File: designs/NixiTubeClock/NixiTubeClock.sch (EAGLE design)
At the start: 14 parts, among them IC1 74141N, IC2 74141N, IC3 74141N, IC4 74141N

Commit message: added nixi tube project
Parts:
- removed V1, V2: 74595N, NixieTube:74595N
- added IC5: 74HCT595D, NixieTube:74HCT595D
- added IC6: 74141N, NixieTube:74141N
- added SV1: (no value), con-lstb:MA08-1
- IC2: value 74141N -> 74HCT595D; device NixieTube:74141N -> NixieTube:74HCT595D
- R1, R2, R3: value (none) -> 12k
- R4: value 68Kh -> (none)
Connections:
- removed net N$1: IC2A.D, V11.QH*
- removed net N$10: IC3A.B, V21.QH
- removed net N$11: IC3A.C, V21.QG
- removed net N$12: IC3A.D, V21.QF
- removed net N$14: IC4A.B, V21.QD
- removed net N$2: IC2A.C, V11.QH
- removed net N$3: IC2A.B, V11.QG
- removed net N$33: AN1.6, IC1A.3
- removed net N$34: AN1.7, IC1A.2
- removed net N$37: AN3.9, IC3A.0
- removed net N$38: AN3.8, IC3A.1
- removed net N$39: AN3.7, IC3A.2
- removed net N$4: IC2A.A, V11.QF
- removed net N$40: AN3.6, IC3A.3
- removed net N$41: AN3.5, IC3A.4
- removed net N$42: AN3.4, IC3A.5
- removed net N$43: AN3.3, IC3A.6
- removed net N$44: AN3.2, IC3A.7
- removed net N$45: AN3.1, IC3A.8
- removed net N$46: AN3.0, IC3A.9
- removed net N$47: AN4.9, IC4A.0
- removed net N$48: AN4.8, IC4A.1
- removed net N$49: AN4.7, IC4A.2
- removed net N$5: IC1A.D, V11.QE
- removed net N$50: AN4.6, IC4A.3
- removed net N$51: AN4.5, IC4A.4
- removed net N$52: AN4.4, IC4A.5
- removed net N$53: AN4.3, IC4A.6
- removed net N$54: AN4.2, IC4A.7
- removed net N$55: AN4.1, IC4A.8
- removed net N$56: AN4.0, IC4A.9
- removed net N$6: IC1A.C, V11.QD
- removed net N$8: IC1A.A, V11.QB
- new net 170V: R1.2, R2.2, R3.2, R4.2, SV1.6
- new net DS: IC2A.SER, SV1.1
- new net N$100: AN4.A1, R4.1
- new net N$101: IC1A.A, IC2A.QA
- new net N$102: IC1A.B, IC2A.QB
- new net N$103: IC1A.C, IC2A.QC
- new net N$104: IC1A.D, IC2A.QD
- new net N$105: IC2A.QE, IC3A.A
- new net N$106: IC2A.QF, IC3A.B
- new net N$107: IC2A.QG, IC3A.C
- new net N$108: IC2A.QH, IC3A.D
- new net N$109: IC4A.A, IC5A.QA
- new net N$110: IC4A.B, IC5A.QB
- new net N$111: IC4A.C, IC5A.QC
- new net N$112: IC5A.QD
- new net N$113: IC5A.QE, IC6A.A
- new net N$114: IC5A.QF, IC6A.B
- new net N$115: IC5A.QG, IC6A.C
- new net N$116: IC5A.QH, IC6A.D
- new net N$66: AN3.3, IC4A.3
- new net N$67: AN3.4, IC4A.4
- new net N$68: AN3.5, IC4A.5
- new net N$69: AN3.6, IC4A.6
- new net N$70: AN3.7, IC4A.7
- new net N$71: AN3.8, IC4A.8
- new net N$72: AN3.9, IC4A.9
- new net N$73: AN4.0, IC6A.0
- new net N$74: AN4.1, IC6A.1
- new net N$75: AN4.2, IC6A.2
- new net N$76: AN4.3, IC6A.3
- new net N$91: AN4.4, IC6A.4
- new net N$92: AN4.5, IC6A.5
- new net N$93: AN4.6, IC6A.6
- new net N$94: AN4.7, IC6A.7
- new net N$95: AN4.8, IC6A.8
- new net N$96: AN4.9, IC6A.9
- new net N$97: AN1.A1, R1.1
- new net N$98: AN2.A1, R2.1
- new net N$99: AN3.A1, R3.1
- new net SHIFT_DATA: IC2A.QH*, IC5A.SER
- new net SH_CP: IC2A.SCK, IC5A.SCK, SV1.2
- new net ST_CP: IC2A.RCK, IC5A.RCK, SV1.3
- new net VCC: SV1.4
- net 5V: now also IC2A.SCL, IC5A.SCL; no longer IC1P.VCC, IC2P.VCC, IC3P.VCC, IC4P.VCC
- net GND: now also IC2A.G, IC5A.G, SV1.5, SV1.7, SV1.8; no longer IC1P.GND, IC2P.GND, IC3P.GND, IC4P.GND
- net N$13: now also AN1.2, IC1A.2; no longer IC4A.A, V21.QE
- net N$15: now also AN1.3, IC1A.3; no longer IC4A.C, V21.QC
- net N$16: now also AN1.4, IC1A.4; no longer IC4A.D, V21.QB
- net N$17: now also AN1.5, IC1A.5; no longer AN2.9, IC2A.0
- net N$18: now also AN1.6, IC1A.6; no longer AN2.8, IC2A.1
- net N$19: now also AN1.7, IC1A.7; no longer AN2.7, IC2A.2
- net N$20: now also AN1.8, IC1A.8; no longer AN2.6, IC2A.3
- net N$21: now also AN1.9, IC1A.9; no longer AN2.5, IC2A.4
- net N$22: now also AN2.0, IC3A.0; no longer AN2.4, IC2A.5
- net N$23: now also AN2.1, IC3A.1; no longer AN2.3, IC2A.6
- net N$24: now also IC3A.2; no longer IC2A.7
- net N$25: now also AN2.3, IC3A.3; no longer AN2.1, IC2A.8
- net N$26: now also AN2.4, IC3A.4; no longer AN2.0, IC2A.9
- net N$27: now also AN2.5, IC3A.5; no longer AN1.0, IC1A.9
- net N$28: now also AN2.6, IC3A.6; no longer AN1.1, IC1A.8
- net N$29: now also AN2.7, IC3A.7; no longer AN1.2, IC1A.7
- net N$30: now also AN2.8, IC3A.8; no longer AN1.3, IC1A.6
- net N$31: now also AN2.9, IC3A.9; no longer AN1.4, IC1A.5
- net N$32: now also AN3.0, IC4A.0; no longer AN1.5, IC1A.4
- net N$35: now also AN3.1, IC4A.1; no longer AN1.8, IC1A.1
- net N$36: now also AN3.2, IC4A.2; no longer AN1.9, IC1A.0
- net N$7: now also AN1.0, IC1A.0; no longer IC1A.B, V11.QC
- net N$9: now also AN1.1, IC1A.1; no longer IC3A.A, V21.QH*
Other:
- note added: "Nothing just Picture"

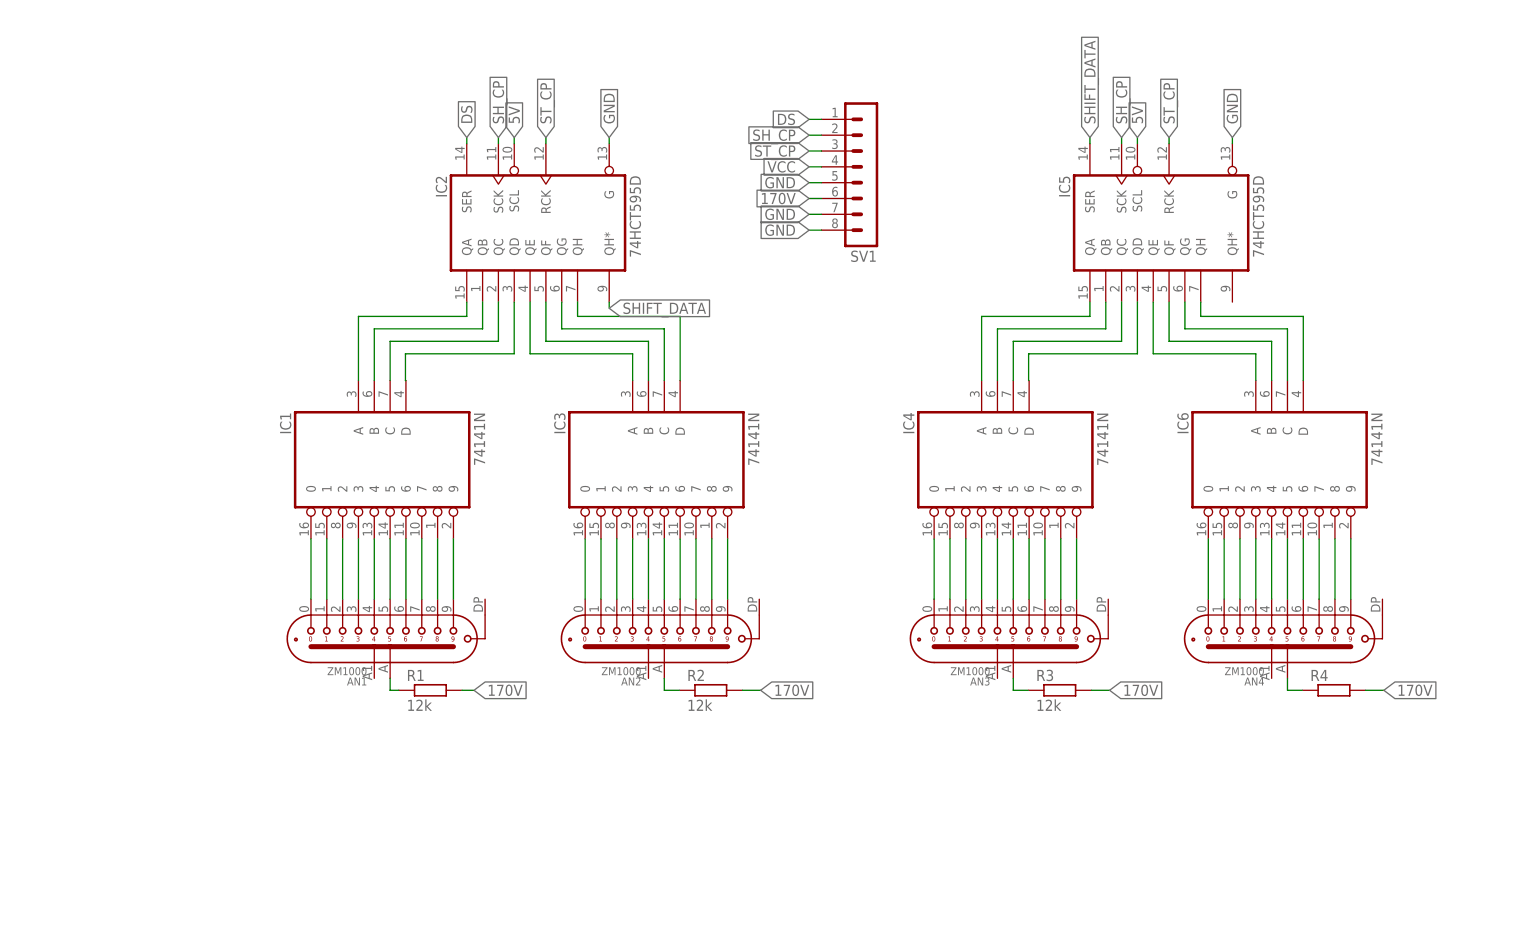
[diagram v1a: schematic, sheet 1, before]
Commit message: added parts for nixi clock final check during the week
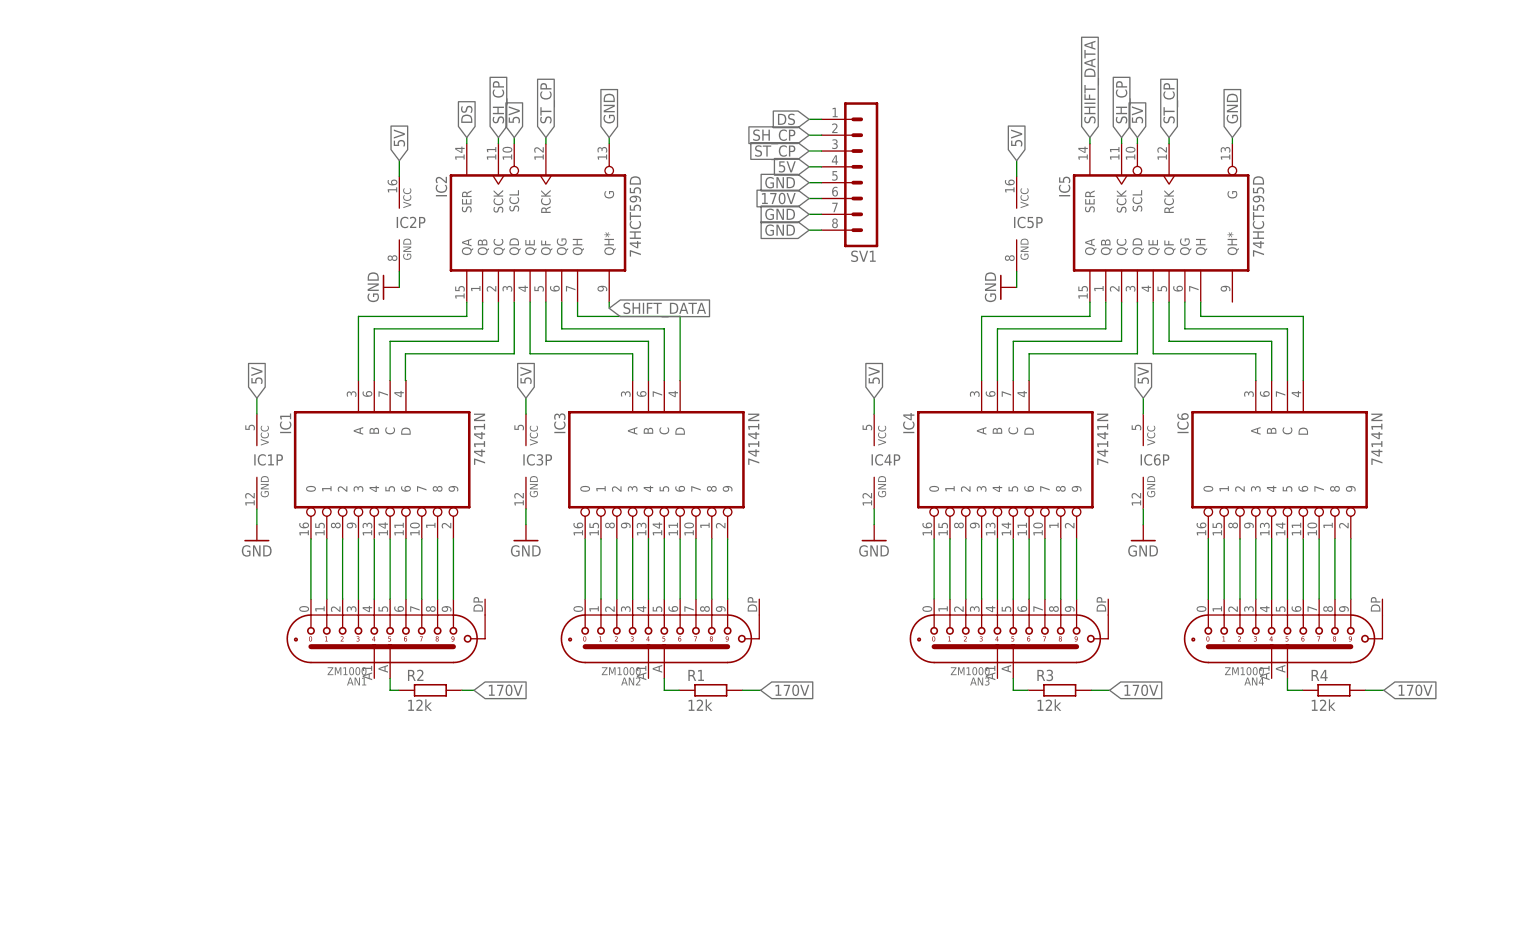
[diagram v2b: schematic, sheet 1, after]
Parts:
- R4: value (none) -> 12k
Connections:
- removed net N$112: IC5A.QD
- removed net VCC: SV1.4
- new net N$1: IC4A.D, IC5A.QD
- net 5V: now also IC1P.VCC, IC2P.VCC, IC3P.VCC, IC4P.VCC, IC5P.VCC, IC6P.VCC, SV1.4
- net GND: now also IC1P.GND, IC2P.GND, IC3P.GND, IC4P.GND, IC5P.GND, IC6P.GND
- net N$97: now also R2.1; no longer R1.1
- net N$98: now also R1.1; no longer R2.1
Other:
- moved on the sheet: R1, R2
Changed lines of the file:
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@@
 <?xml version="1.0" encoding="utf-8"?>
 <!DOCTYPE eagle SYSTEM "eagle.dtd">
-<eagle version="9.4.2">
+<eagle version="9.5.1">
 <drawing>
 <settings>
@@
 <part name="IC3" library="NixieTube" deviceset="74*141" device="N" package3d_urn="urn:adsk.eagle:package:922/2"/>
 <part name="IC1" library="NixieTube" deviceset="74*141" device="N" package3d_urn="urn:adsk.eagle:package:922/2"/>
+<part name="R2" library="CommonParts" deviceset="R-EU_1206" device="R1206" package3d_urn="urn:adsk.eagle:package:23540/2" value="12k"/>
 <part name="R1" library="CommonParts" deviceset="R-EU_1206" device="R1206" package3d_urn="urn:adsk.eagle:package:23540/2" value="12k"/>
-<part name="R2" library="CommonParts" deviceset="R-EU_1206" device="R1206" package3d_urn="urn:adsk.eagle:package:23540/2" value="12k"/>
 <part name="R3" library="CommonParts" deviceset="R-EU_1206" device="R1206" package3d_urn="urn:adsk.eagle:package:23540/2" value="12k"/>
-<part name="R4" library="CommonParts" deviceset="R-EU_1206" device="R1206" package3d_urn="urn:adsk.eagle:package:23540/2"/>
+<part name="R4" library="CommonParts" deviceset="R-EU_1206" device="R1206" package3d_urn="urn:adsk.eagle:package:23540/2" value="12k"/>
 <part name="IC2" library="NixieTube" deviceset="74*595" device="D" package3d_urn="urn:adsk.eagle:package:2010/1" technology="HCT" value="74HCT595D"/>
 <part name="IC5" library="NixieTube" deviceset="74*595" device="D" package3d_urn="urn:adsk.eagle:package:2010/1" technology="HCT" value="74HCT595D"/>
+<part name="GND1" library="supply1" library_urn="urn:adsk.eagle:library:371" deviceset="GND" device=""/>
+<part name="GND2" library="supply1" library_urn="urn:adsk.eagle:library:371" deviceset="GND" device=""/>
+<part name="GND3" library="supply1" library_urn="urn:adsk.eagle:library:371" deviceset="GND" device=""/>
+<part name="GND4" library="supply1" library_urn="urn:adsk.eagle:library:371" deviceset="GND" device=""/>
+<part name="GND5" library="supply1" library_urn="urn:adsk.eagle:library:371" deviceset="GND" device=""/>
+<part name="GND6" library="supply1" library_urn="urn:adsk.eagle:library:371" deviceset="GND" device=""/>
 </parts>
 <sheets>
@@
 <attribute name="VALUE" x="46.78" y="53.62" size="1.778" layer="96" rot="MR270"/>
 </instance>
-<instance part="R1" gate="G$1" x="38" y="9" smashed="yes">
+<instance part="R2" gate="G$1" x="38" y="9" smashed="yes">
 <attribute name="NAME" x="34.19" y="10.4986" size="1.778" layer="95"/>
 <attribute name="VALUE" x="34.19" y="5.698" size="1.778" layer="96"/>
 </instance>
-<instance part="R2" gate="G$1" x="83" y="9" smashed="yes">
+<instance part="R1" gate="G$1" x="83" y="9" smashed="yes">
 <attribute name="NAME" x="79.19" y="10.4986" size="1.778" layer="95"/>
 <attribute name="VALUE" x="79.19" y="5.698" size="1.778" layer="96"/>
@@
 <attribute name="NAME" x="140.665" y="91.62" size="1.778" layer="95" rot="MR270"/>
 <attribute name="VALUE" x="171.78" y="91.62" size="1.778" layer="96" rot="MR270"/>
+</instance>
+<instance part="IC1" gate="P" x="10.16" y="45.72" smashed="yes">
+<attribute name="NAME" x="9.525" y="45.085" size="1.778" layer="95"/>
+</instance>
+<instance part="IC3" gate="P" x="53.34" y="45.72" smashed="yes">
+<attribute name="NAME" x="52.705" y="45.085" size="1.778" layer="95"/>
+</instance>
+<instance part="IC4" gate="P" x="109.22" y="45.72" smashed="yes">
+<attribute name="NAME" x="108.585" y="45.085" size="1.778" layer="95"/>
+</instance>
+<instance part="IC6" gate="P" x="152.4" y="45.72" smashed="yes">
+<attribute name="NAME" x="151.765" y="45.085" size="1.778" layer="95"/>
+</instance>
+<instance part="IC5" gate="P" x="132.08" y="83.82" smashed="yes">
+<attribute name="NAME" x="131.445" y="83.185" size="1.778" layer="95"/>
+</instance>
+<instance part="IC2" gate="P" x="33.02" y="83.82" smashed="yes">
+<attribute name="NAME" x="32.385" y="83.185" size="1.778" layer="95"/>
+</instance>
+<instance part="GND1" gate="1" x="10.16" y="33.02" smashed="yes">
+<attribute name="VALUE" x="7.62" y="30.48" size="1.778" layer="96"/>
+</instance>
+<instance part="GND2" gate="1" x="53.34" y="33.02" smashed="yes">
+<attribute name="VALUE" x="50.8" y="30.48" size="1.778" layer="96"/>
+</instance>
+<instance part="GND3" gate="1" x="109.22" y="33.02" smashed="yes">
+<attribute name="VALUE" x="106.68" y="30.48" size="1.778" layer="96"/>
+</instance>
+<instance part="GND4" gate="1" x="152.4" y="33.02" smashed="yes">
+<attribute name="VALUE" x="149.86" y="30.48" size="1.778" layer="96"/>
+</instance>
+<instance part="GND5" gate="1" x="129.54" y="73.66" smashed="yes" rot="R270">
+<attribute name="VALUE" x="127" y="76.2" size="1.778" layer="96" rot="R270"/>
+</instance>
+<instance part="GND6" gate="1" x="30.48" y="73.66" smashed="yes" rot="R270">
+<attribute name="VALUE" x="27.94" y="76.2" size="1.778" layer="96" rot="R270"/>
 </instance>
 </instances>
@@
 <label x="98.78" y="82.84" size="1.778" layer="95" rot="R180" xref="yes"/>
 </segment>
+<segment>
+<pinref part="IC1" gate="P" pin="GND"/>
+<wire x1="10.16" y1="38.1" x2="10.16" y2="35.56" width="0.1524" layer="91"/>
+<pinref part="GND1" gate="1" pin="GND"/>
+</segment>
+<segment>
+<pinref part="IC3" gate="P" pin="GND"/>
+<wire x1="53.34" y1="38.1" x2="53.34" y2="35.56" width="0.1524" layer="91"/>
+<pinref part="GND2" gate="1" pin="GND"/>
+</segment>
+<segment>
+<pinref part="IC4" gate="P" pin="GND"/>
+<wire x1="109.22" y1="38.1" x2="109.22" y2="35.56" width="0.1524" layer="91"/>
+<pinref part="GND3" gate="1" pin="GND"/>
+</segment>
+<segment>
+<pinref part="IC6" gate="P" pin="GND"/>
+<wire x1="152.4" y1="38.1" x2="152.4" y2="35.56" width="0.1524" layer="91"/>
+<pinref part="GND4" gate="1" pin="GND"/>
+</segment>
+<segment>
+<pinref part="IC5" gate="P" pin="GND"/>
+<wire x1="132.08" y1="76.2" x2="132.08" y2="73.66" width="0.1524" layer="91"/>
+<pinref part="GND5" gate="1" pin="GND"/>
+</segment>
+<segment>
+<pinref part="IC2" gate="P" pin="GND"/>
+<wire x1="33.02" y1="76.2" x2="33.02" y2="73.66" width="0.1524" layer="91"/>
+<pinref part="GND6" gate="1" pin="GND"/>
+</segment>
 </net>
 <net name="5V" class="0">
@@
 <label x="151.46" y="97.7" size="1.778" layer="95" rot="R90" xref="yes"/>
 </segment>
+<segment>
+<pinref part="IC5" gate="P" pin="VCC"/>
+<wire x1="132.08" y1="91.44" x2="132.08" y2="93.98" width="0.1524" layer="91"/>
+<label x="132.08" y="93.98" size="1.778" layer="95" rot="R90" xref="yes"/>
+</segment>
+<segment>
+<pinref part="IC2" gate="P" pin="VCC"/>
+<wire x1="33.02" y1="91.44" x2="33.02" y2="93.98" width="0.1524" layer="91"/>
+<label x="33.02" y="93.98" size="1.778" layer="95" rot="R90" xref="yes"/>
+</segment>
+<segment>
+<pinref part="IC1" gate="P" pin="VCC"/>
+<wire x1="10.16" y1="53.34" x2="10.16" y2="55.88" width="0.1524" layer="91"/>
+<label x="10.16" y="55.88" size="1.778" layer="95" rot="R90" xref="yes"/>
+</segment>
+<segment>
+<pinref part="IC3" gate="P" pin="VCC"/>
+<wire x1="53.34" y1="53.34" x2="53.34" y2="55.88" width="0.1524" layer="91"/>
+<label x="53.34" y="55.88" size="1.778" layer="95" rot="R90" xref="yes"/>
+</segment>
+<segment>
+<pinref part="IC4" gate="P" pin="VCC"/>
+<wire x1="109.22" y1="53.34" x2="109.22" y2="55.88" width="0.1524" layer="91"/>
+<label x="109.22" y="55.88" size="1.778" layer="95" rot="R90" xref="yes"/>
+</segment>
+<segment>
+<pinref part="IC6" gate="P" pin="VCC"/>
+<wire x1="152.4" y1="53.34" x2="152.4" y2="55.88" width="0.1524" layer="91"/>
+<label x="152.4" y="55.88" size="1.778" layer="95" rot="R90" xref="yes"/>
+</segment>
+<segment>
+<pinref part="SV1" gate="1" pin="4"/>
+<wire x1="100.78" y1="93" x2="98.78" y2="93" width="0.1524" layer="91"/>
+<label x="98.78" y="93" size="1.778" layer="95" rot="R180" xref="yes"/>
+</segment>
 </net>
 <net name="N$7" class="0">
@@
 <pinref part="AN1" gate="G$1" pin="A1"/>
 <wire x1="31.54" y1="10.92" x2="31.54" y2="9" width="0.1524" layer="91"/>
+<pinref part="R2" gate="G$1" pin="1"/>
+<wire x1="31.54" y1="9" x2="32.92" y2="9" width="0.1524" layer="91"/>
+</segment>
+</net>
+<net name="N$98" class="0">
+<segment>
 <pinref part="R1" gate="G$1" pin="1"/>
-<wire x1="31.54" y1="9" x2="32.92" y2="9" width="0.1524" layer="91"/>
-</segment>
-</net>
-<net name="N$98" class="0">
-<segment>
-<pinref part="R2" gate="G$1" pin="1"/>
 <pinref part="AN2" gate="G$1" pin="A1"/>
 <wire x1="77.92" y1="9" x2="75.54" y2="9" width="0.1524" layer="91"/>
@@
 </segment>
 </net>
-<net name="N$112" class="0">
-<segment>
-<wire x1="151.46" y1="71.3" x2="151.46" y2="63" width="0.1524" layer="91"/>
-<wire x1="151.46" y1="63" x2="134" y2="63" width="0.1524" layer="91"/>
-<wire x1="134" y1="63" x2="134" y2="58.7" width="0.1524" layer="91"/>
-<pinref part="IC5" gate="A" pin="QD"/>
-</segment>
-</net>
 <net name="N$113" class="0">
 <segment>
@@
 <net name="170V" class="0">
 <segment>
-<pinref part="R1" gate="G$1" pin="2"/>
+<pinref part="R2" gate="G$1" pin="2"/>
 <wire x1="43.08" y1="9" x2="45" y2="9" width="0.1524" layer="91"/>
 <label x="45" y="9" size="1.778" layer="95" xref="yes"/>
 </segment>
 <segment>
-<pinref part="R2" gate="G$1" pin="2"/>
+<pinref part="R1" gate="G$1" pin="2"/>
 <wire x1="88.08" y1="9" x2="91" y2="9" width="0.1524" layer="91"/>
 <label x="91" y="9" size="1.778" layer="95" xref="yes"/>
@@
 </segment>
 </net>
-<net name="VCC" class="0">
-<segment>
-<pinref part="SV1" gate="1" pin="4"/>
-<wire x1="100.78" y1="93" x2="98.78" y2="93" width="0.1524" layer="91"/>
-<label x="98.78" y="93" size="1.778" layer="95" rot="R180" xref="yes"/>
-</segment>
-</net>
+<net name="N$1" class="0">
+<segment>
+<pinref part="IC4" gate="A" pin="D"/>
+<wire x1="134.08" y1="58.7" x2="134.08" y2="63" width="0.1524" layer="91"/>
+<wire x1="134.08" y1="63" x2="151.46" y2="63" width="0.1524" layer="91"/>
+<pinref part="IC5" gate="A" pin="QD"/>
+<wire x1="151.46" y1="63" x2="151.46" y2="71.3" width="0.1524" layer="91"/>
+</segment>
+</net>

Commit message: added new nixi clock design top board
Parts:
- removed SV1: (no value), con-lstb:MA08-1
- added JP1: (no value), pinhead:PINHD-2X4/90
- added JP3: (no value), pinhead:PINHD-2X5/90
- added SV2: (no value), con-lstb:MA12-1
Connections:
- new net 12V: JP1.8, SV2.11
- new net DS1: IC2A.SER, JP3.1, SV2.4
- new net DS2: JP3.2, SV2.7
- new net SCL1: JP3.3, SV2.6
- new net SCL2: JP3.4, SV2.9
- new net SDA1: JP3.5, SV2.5
- new net SDA2: JP3.6, SV2.8
- net 170V: now also JP1.1; no longer SV1.6
- net 5V: now also JP3.7, JP3.8, SV2.12; no longer SV1.4
- net DS: now also SV2.1; no longer IC2A.SER, SV1.1
- net GND: now also JP1.2, JP1.3, JP1.4, JP1.5, JP1.6, JP1.7, JP3.10, JP3.9, SV2.10; no longer SV1.5, SV1.7, SV1.8
- net SH_CP: now also SV2.2; no longer SV1.2
- net ST_CP: now also SV2.3; no longer SV1.3
